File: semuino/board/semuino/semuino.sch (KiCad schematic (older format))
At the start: 34 parts, among them J1 bpc_pwr_10A, J10 Conn_01x02, J11 Conn_01x02, J12 Conn_01x02, J13 Conn_01x02, J2 bpc_pwr_10A, J3 bpc_pwr_5A, J4 bpc_pwr_5A, J5 bpc_pwr_5A, J6 bpc_pwr_5A, J7 Conn_01x03, J8 Conn_01x03, J9 Conn_01x03, Q1 TIP41C, Q2 TIP41C, Q3 TIP41C, Q4 TIP41C

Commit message: Carte de commande éclairage semi
- Alim 12V/10A
- 3 sorties 12V/2A
- 3 sorties RGB 5V/2A
- RTC
- Sonde température
- extension ESP 01 Wifi
- 1 entrée select
- 1 entrée ON/OFF pour ESP 01
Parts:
- removed A1: Arduino_Nano_v3.x, bpc:BPC_Arduino_Nano, symbol bpc_scm:Arduino_Nano_v3.x
- removed J1, J2: bpc_pwr_10A, bpc:BPC_PWR_10A, symbol bpc_scm:bpc_pwr_10A
- removed J3, J4, J5, J6: bpc_pwr_5A, bpc:BPC_PWR_5A, symbol bpc_scm:bpc_pwr_5A
- removed Q1, Q3, Q4: TIP41C, Package_TO_SOT_THT:TO-220-3_Vertical, symbol Transistor_BJT:TIP41C
- added A1: Arduino_Nano_v2.x, bpc:BPC_Arduino_Nano, symbol bpc:Arduino_Nano_v2.x
- added J1, J3: Conn_01x02, TerminalBlock_Phoenix:TerminalBlock_Phoenix_MKDS-1,5-2_1x02_P5.00mm_Horizontal, symbol Connector_Generic:Conn_01x02
- added J11: Conn_01x02, Connector_PinHeader_2.54mm:PinHeader_1x02_P2.54mm_Vertical, symbol Connector_Generic:Conn_01x02
- added J4: Conn_01x02, TerminalBlock_Phoenix:TerminalBlock_Phoenix_MPT-0,5-2-2.54_1x02_P2.54mm_Horizontal, symbol Connector_Generic:Conn_01x02
- added Q1, Q4, Q5: 2N2222A, Package_TO_SOT_THT:TO-18-3, symbol Transistor_BJT:2N2222A
- added Q2, Q6, Q7, Q8: P03P4L-04, Package_TO_SOT_THT:TO-220-3_Vertical, symbol bpc:P03P4L-04
- added R12: 100, Resistor_THT:R_Axial_DIN0309_L9.0mm_D3.2mm_P2.54mm_Vertical, symbol Device:R
- added R13, R14, R3, R4, R5: 100k, Resistor_THT:R_Axial_DIN0309_L9.0mm_D3.2mm_P2.54mm_Vertical, symbol Device:R
- added U1: RtcArduino, bpc:BPC_RtcArduino, symbol bpc:RtcArduino
- added U2: BPC_ESP8266-01_ESP-01, bpc:BPC_XCVR_ESP8266-01_ESP-01, symbol bpc:BPC_ESP8266-01_ESP-01
- added U3: BPC_DHT22, bpc:BPC_DHT22, symbol bpc:BPC_DHT22
- F3, F4, F5, F6, F7, F8: footprint Fuse:Fuseholder_Cylinder-5x20mm_Schurter_0031_8201_Horizontal_Open -> Fuse:Fuseholder_TR5_Littelfuse_No560_No460
- J5: renamed from J7; footprint TerminalBlock_Phoenix:TerminalBlock_Phoenix_MKDS-1,5-3-5.08_1x03_P5.08mm_Horizontal -> TerminalBlock_Phoenix:TerminalBlock_Phoenix_MPT-0,5-3-2.54_1x03_P2.54mm_Horizontal
- J6: renamed from J8; footprint TerminalBlock_Phoenix:TerminalBlock_Phoenix_MKDS-1,5-3-5.08_1x03_P5.08mm_Horizontal -> TerminalBlock_Phoenix:TerminalBlock_Phoenix_MPT-0,5-3-2.54_1x03_P2.54mm_Horizontal
- J7: renamed from J9; footprint TerminalBlock_Phoenix:TerminalBlock_Phoenix_MKDS-1,5-3-5.08_1x03_P5.08mm_Horizontal -> TerminalBlock_Phoenix:TerminalBlock_Phoenix_MPT-0,5-3-2.54_1x03_P2.54mm_Horizontal
- Q3: renamed from Q2; value TIP41C -> 2N2222A; footprint Package_TO_SOT_THT:TO-220-3_Vertical -> Package_TO_SOT_THT:TO-18-3; symbol Transistor_BJT:TIP41C -> Transistor_BJT:2N2222A; Arrow Part Number (none) -> 2N2222A; Arrow Price/Stock (none) -> https://www.arrow.com/en/products/2n2222a/microsemi; Description (none) -> Trans GP BJT NPN 50V 0.8A 3-Pin TO-18; Manufacturer_Name (none) -> Microsemi Corporation; Manufacturer_Part_Number (none) -> 2N2222A; Mouser Part Number (none) -> 494-2N2222A; Mouser Price/Stock (none) -> https://www.mouser.co.uk/ProductDetail/Microchip-Microsemi/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
- R1: value 50 -> 100
- renumbered J12 to J10, J13 to J2, J10 to J8, J11 to J9, R7 to R10, R8 to R11, R3 to R6, R4 to R7, R5 to R8, R6 to R9
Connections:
- net labels added: 3.3V, NanoRX, NanoTx, PWR_5V, SCL, SDA, Temp, Vcc, Vin
- wire segments 84 -> 161
- no-connect marks 0 -> 14
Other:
- moved on the sheet: F3, F4, F5, F6, F7, F8, J10, J2, J5, J6, J7, J8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

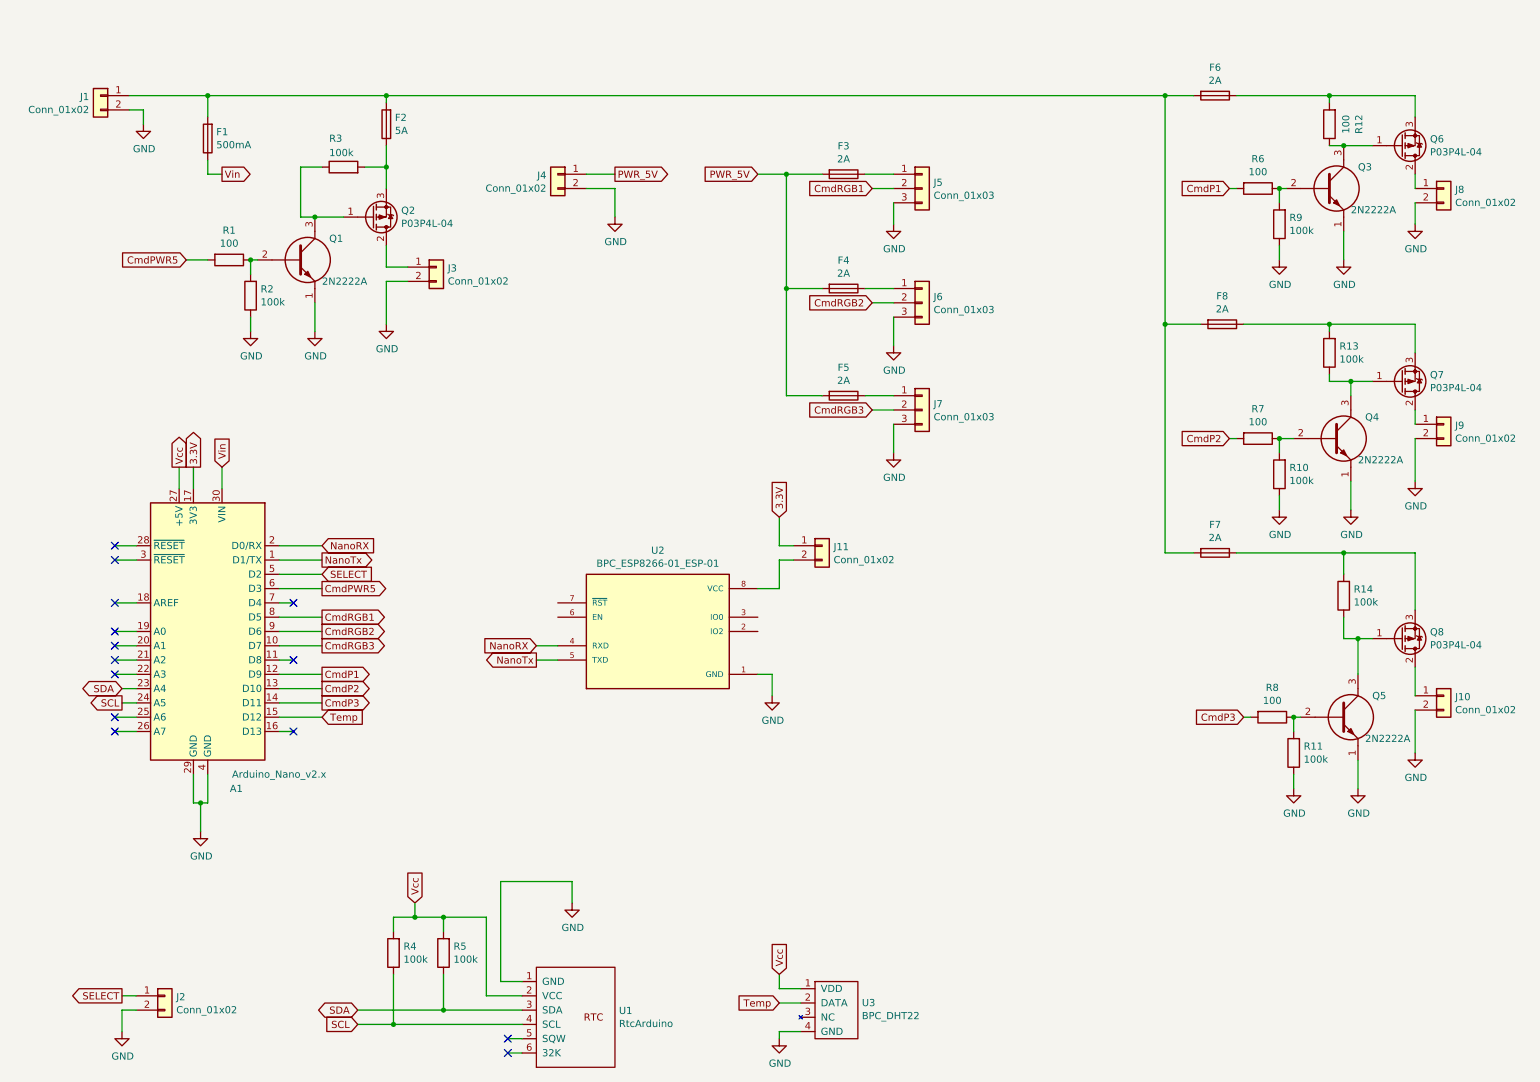
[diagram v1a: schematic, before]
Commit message: SEMUINO: Rework de la carte
- 3 LEDs 12V
- 3 LEDs RGB (avec R de protection sur data)
- 3 capteurs humidité sol
- 1 Connecteur pour écran OLED
- 1 RTC
- 1 ESP01 pour le Wifi
- Des fusibles
- carte au format boîte de dérivation
- ...
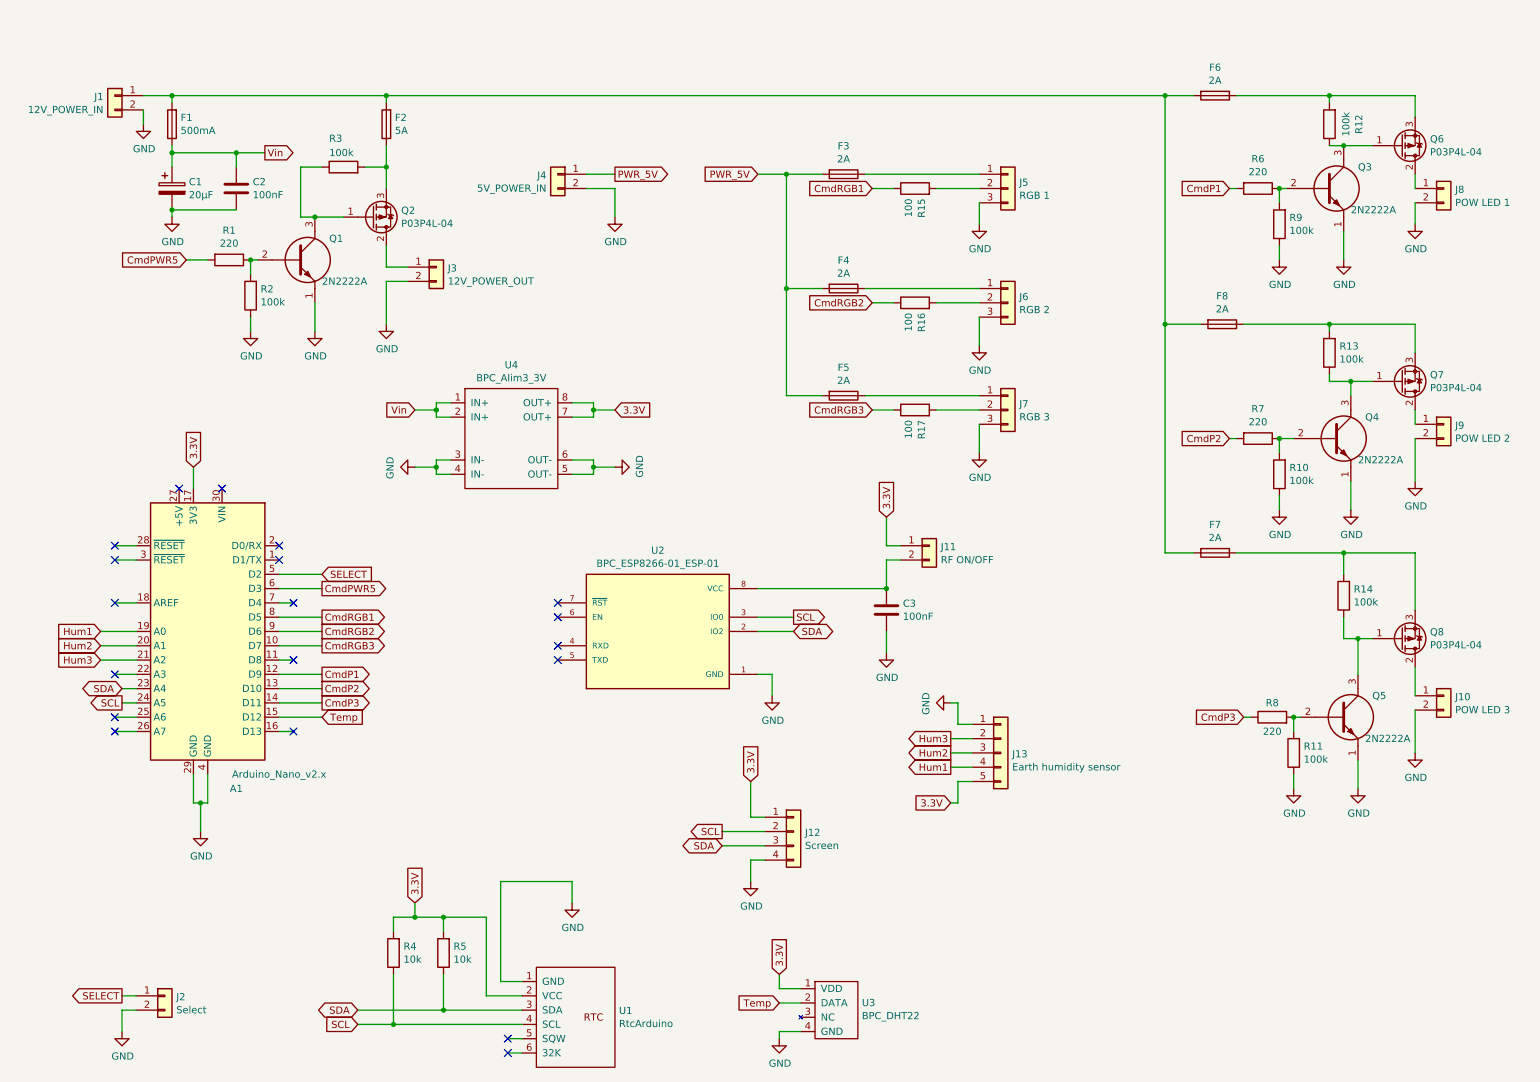
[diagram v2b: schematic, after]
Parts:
- added C1: 20µF, Capacitor_THT:CP_Radial_D8.0mm_P3.80mm, symbol Device:CP
- added C2, C3: 100nF, Capacitor_THT:C_Disc_D7.0mm_W2.5mm_P5.00mm, symbol Device:C
- added J12: Screen, Connector_JST:JST_XH_B4B-XH-A_1x04_P2.50mm_Vertical, symbol Connector_Generic:Conn_01x04
- added J13: Earth humidity sensor, TerminalBlock_Phoenix:TerminalBlock_Phoenix_MPT-0,5-5-2.54_1x05_P2.54mm_Horizontal, symbol Connector_Generic:Conn_01x05
- added R15, R16, R17: 100, Resistor_THT:R_Axial_DIN0309_L9.0mm_D3.2mm_P2.54mm_Vertical, symbol Device:R
- added U4: BPC_Alim3_3V, bpc:BPC_Alim3_3V, symbol bpc:BPC_Alim3_3V
- J1: value Conn_01x02 -> 12V_POWER_IN
- J10: value Conn_01x02 -> POW LED 3
- J11: value Conn_01x02 -> RF ON/OFF
- J2: value Conn_01x02 -> Select
- J3: value Conn_01x02 -> 12V_POWER_OUT
- J4: value Conn_01x02 -> 5V_POWER_IN
- J5: value Conn_01x03 -> RGB 1
- J6: value Conn_01x03 -> RGB 2
- J7: value Conn_01x03 -> RGB 3
- J8: value Conn_01x02 -> POW LED 1
- J9: value Conn_01x02 -> POW LED 2
- Q1, Q3, Q4, Q5: footprint Package_TO_SOT_THT:TO-18-3 -> Package_TO_SOT_THT:TO-92
- R1, R6, R7, R8: value 100 -> 220
- R12: value 100 -> 100k
- R4, R5: value 100k -> 10k; footprint Resistor_THT:R_Axial_DIN0309_L9.0mm_D3.2mm_P2.54mm_Vertical -> Resistor_THT:R_Axial_DIN0309_L9.0mm_D3.2mm_P12.70mm_Horizontal
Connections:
- net 3.3V: now also R4.2, R5.2, U1.2 (VCC), U3.1 (VDD), J12.1 (Pin_1), J13.5 (Pin_5), U4.7 (OUT+), U4.8 (OUT+)
- net CmdP3: now also R8.1; no longer R8.2
- net CmdRGB1: now also R15.1; no longer J5.2 (Pin_2)
- net CmdRGB2: now also R16.1; no longer J6.2 (Pin_2)
- net CmdRGB3: now also R17.1; no longer J7.2 (Pin_2)
- net GND: now also C1.2, C2.2, C3.2, J12.4 (Pin_4), J13.1 (Pin_1), U4.3 (IN-), U4.4 (IN-), U4.5 (OUT-), U4.6 (OUT-)
- net SCL: now also U2.3 (IO0), J12.2 (Pin_2)
- net SDA: now also U2.2 (IO2), J12.3 (Pin_3)
- net Vin: now also C1.1, C2.1, U4.1 (IN+), U4.2 (IN+); no longer A1.30 (VIN)
- net at Q5.2, R11.2: now also R8.2; no longer R8.1
- net Hum1: now reaches A1.19 (A0)
- net Hum1: now also J13.4 (Pin_4)
- net Hum2: now reaches A1.20 (A1)
- net Hum2: now also J13.3 (Pin_3)
- net Hum3: now reaches A1.21 (A2)
- net Hum3: now also J13.2 (Pin_2)
- net at J11.2 (Pin_2), U2.8 (VCC): now also C3.1
- net NanoRX: no longer names the net of A1.2 (D0/RX)
- net NanoRX: no longer U2.4 (RXD)
- net NanoTx: no longer names the net of A1.1 (D1/TX)
- net NanoTx: no longer U2.5 (TXD)
- removed net Vcc: A1.27 (+5V), R4.2, R5.2, U1.2 (VCC), U3.1 (VDD)
- new net: J5.2 (Pin_2), R15.2
- new net: J6.2 (Pin_2), R16.2
- new net: J7.2 (Pin_2), R17.2
- no-connect marks 14 -> 19
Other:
- moved on the sheet: F1, J1, J11, J5, J6, J7
